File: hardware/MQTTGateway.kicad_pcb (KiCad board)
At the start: 2 copper layers, 284 parts, among them J1 Screw_Terminal_01x02, J10 Screw_Terminal_01x03, J11 Screw_Terminal_01x03, J12 Screw_Terminal_01x03, J13 Screw_Terminal_01x03, J14 Screw_Terminal_01x03, J15 Screw_Terminal_01x03, J16 Screw_Terminal_01x03, J17 Screw_Terminal_01x03, J18 Screw_Terminal_01x03, J19 Screw_Terminal_01x03, J2 RJ45_Amphenol_RJMG1BD3B8K1ANR, J20 Screw_Terminal_01x03, J21 Screw_Terminal_01x03, J22 Screw_Terminal_01x02, J23 Screw_Terminal_01x02, J24 Screw_Terminal_01x02, J25 Screw_Terminal_01x02, J3 Screw_Terminal_01x03, J4 Screw_Terminal_01x02, J5 Screw_Terminal_01x02, J6 Screw_Terminal_01x02, J7 Screw_Terminal_01x02, J8 Screw_Terminal_01x02, J9 Screw_Terminal_01x02, K1 G2RL-2, K2 G2RL-2, K3 G2RL-2, K4 G2RL-2, Q1 2N7002, Q2 2N7002, Q3 2N7002, Q4 2N7002, Q5 2N7002, Q6 2N7002, Q7 2N7002, Q8 2N7002, Q9 2N7002, SW1 SW_Push, U1 K78xx, U11 MCP6004, U15 LTV-847S, U2 AMS1117CD-3.3, U3 STM32F407VETx, U4 W25Q128JVS, U5 LAN8720A, U6 ESP32-WROOM-32E, U7 MAX3232, U8 SP3485CN, U9 SN65HVD230, Y1 8MHz, Y2 32.768 KHz, Y3 25MHz

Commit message: More improvements
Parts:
- removed U11 (x2): MCP6004, Package_DIP:SMDIP-16_W9.53mm
- added U10: MCP6004, Package_SO:SOIC-14_3.9x8.7mm_P1.27mm, F.Cu at (164.5, 148.4)
- moved D4 5.86 mm to (114.2, 105.2)

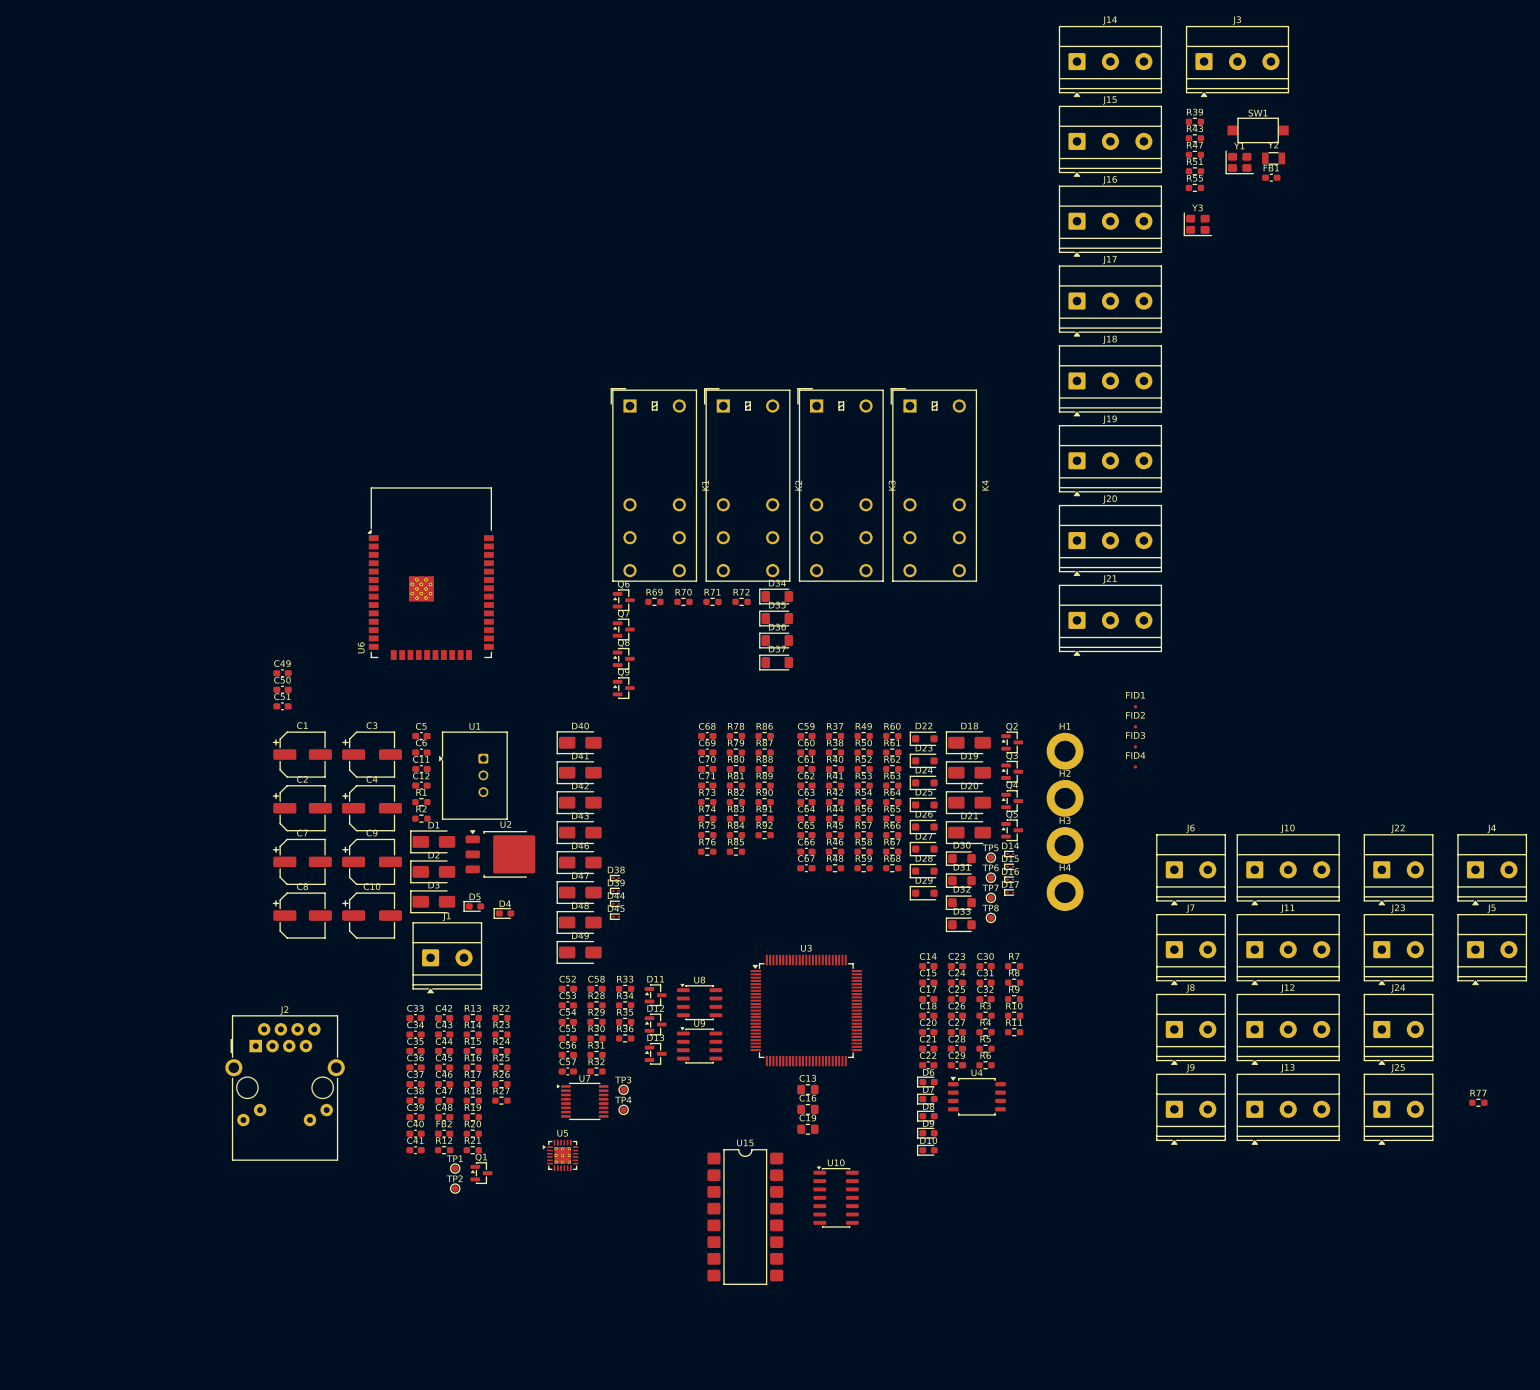
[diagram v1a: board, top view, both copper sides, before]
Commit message: Make connectors DB9
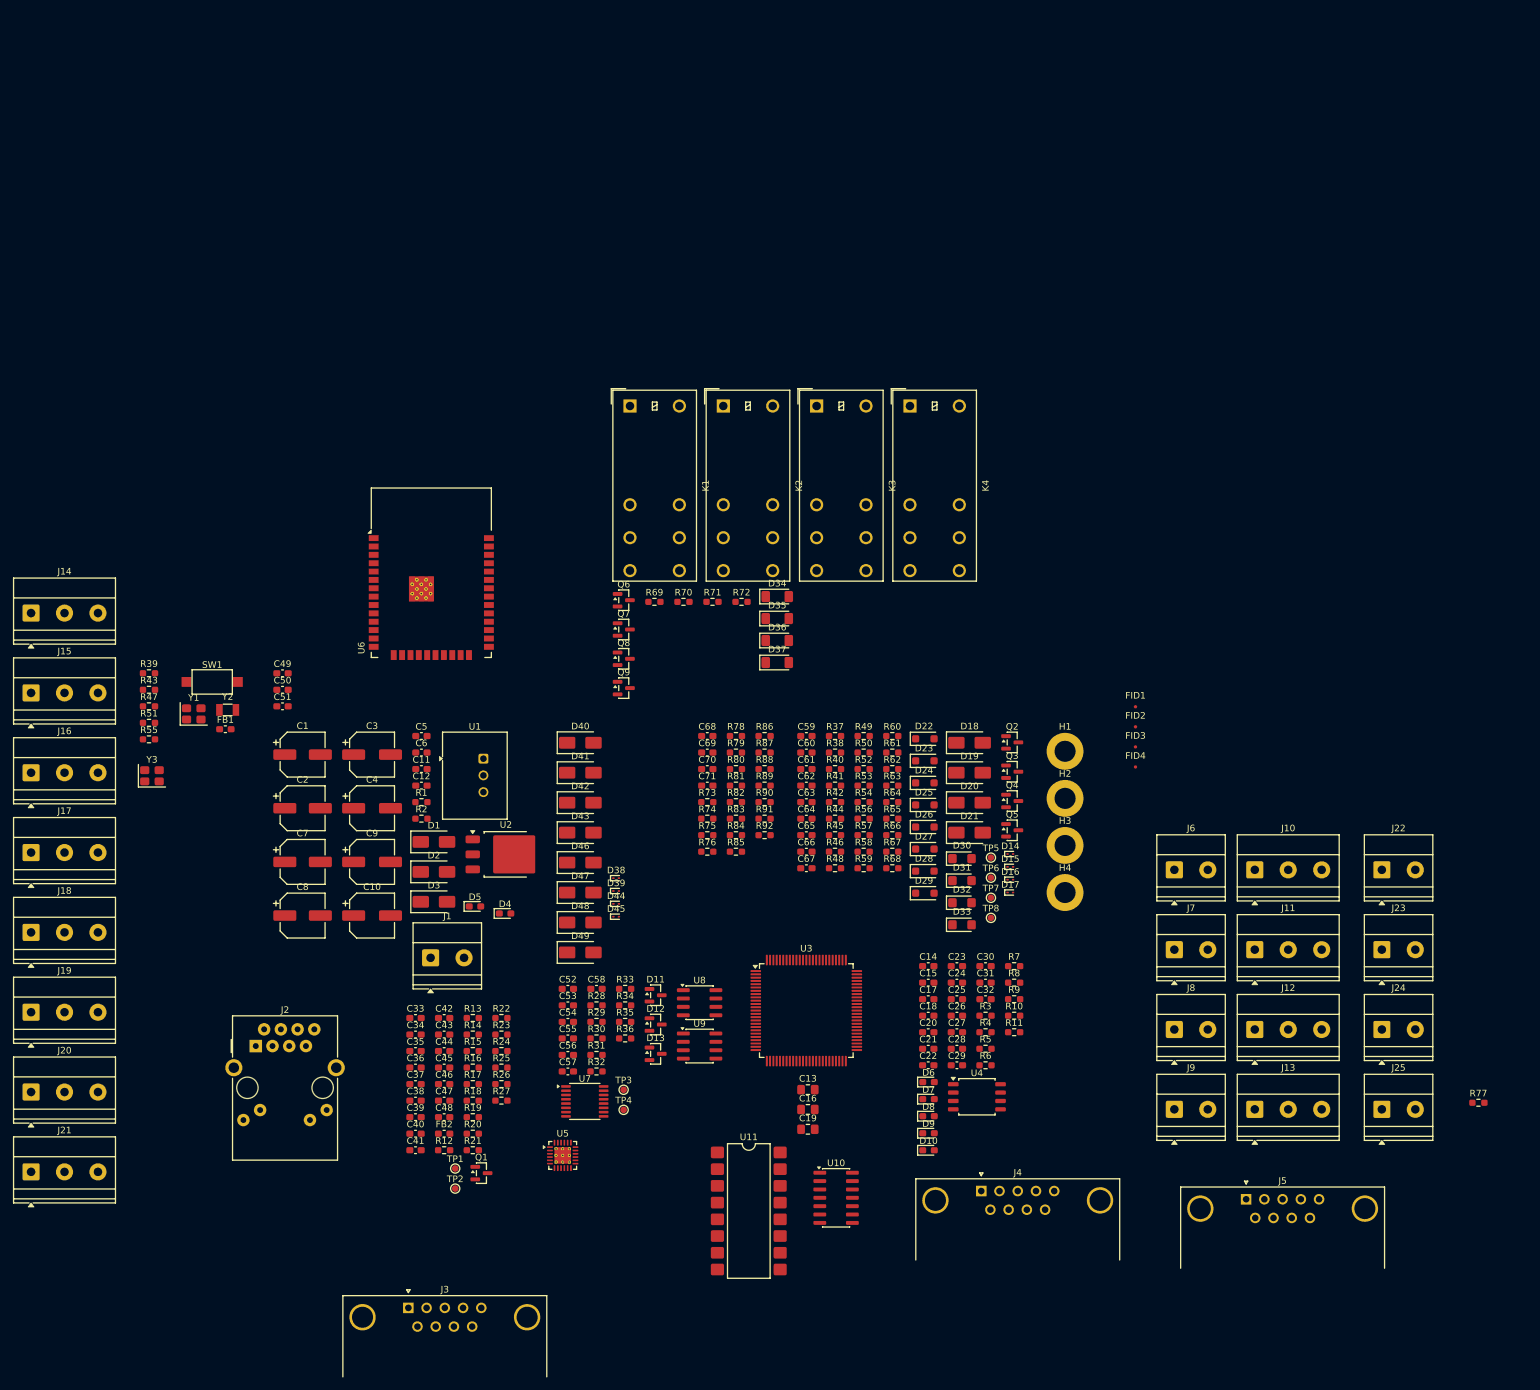
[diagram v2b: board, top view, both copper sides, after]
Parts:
- removed U15: LTV-847S, Package_DIP:SMDIP-16_W9.53mm
- added U11: LTV-847S, Package_DIP:SMDIP-16_W9.53mm, F.Cu at (151.3, 150.4)
- J3: value Screw_Terminal_01x03 -> DE9_Pins_MountingHoles; footprint TerminalBlock_Phoenix:TerminalBlock_Phoenix_MKDS-1,5-3-5.08_1x03_P5.08mm_Horizontal -> Connector_Dsub:DSUB-9_Pins_Horizontal_P2.77x2.84mm_EdgePinOffset7.70mm_Housed_MountingHolesOffset9.12mm
- J4, J5: value Screw_Terminal_01x02 -> DE9_Pins_MountingHoles; footprint TerminalBlock_Phoenix:TerminalBlock_Phoenix_MKDS-1,5-2-5.08_1x02_P5.08mm_Horizontal -> Connector_Dsub:DSUB-9_Pins_Horizontal_P2.77x2.84mm_EdgePinOffset7.70mm_Housed_MountingHolesOffset9.12mm
- moved J3 224.6 mm to (99.6, 165.2)
- moved FB1 179.6 mm to (71.8, 77.3)
- moved J14 179.6 mm to (42.2, 59.6)
- moved J15 179.6 mm to (42.2, 71.8)
- moved J16 179.6 mm to (42.2, 83.9)
- moved J17 179.6 mm to (42.2, 96.0)
- moved J18 179.6 mm to (42.2, 108.1)
- moved J19 179.6 mm to (42.2, 120.2)
- moved J20 179.6 mm to (42.2, 132.4)
- moved J21 179.6 mm to (42.2, 144.5)
- moved R39 179.6 mm to (60.2, 68.8)
- moved R43 179.6 mm to (60.2, 71.3)
- moved R47 179.6 mm to (60.2, 73.8)
- moved R51 179.6 mm to (60.2, 76.3)
- moved R55 179.6 mm to (60.2, 78.8)
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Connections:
- D11 pad 1: Net-(J3-Pin_1) -> /Peripherals/RS232_TX
- D11 pad 2: Net-(J3-Pin_3) -> /Peripherals/RS232_RX
- D12 pad 1: Net-(J4-Pin_1) -> /Peripherals/CAN_HIGH_P
- D12 pad 2: Net-(J4-Pin_2) -> /Peripherals/CAN_LOW_N
- D13 pad 1: Net-(D13-A1) -> /Peripherals/RS485_P
- D13 pad 2: Net-(D13-A2) -> /Peripherals/RS485_N
- J3 pad 1: Net-(J3-Pin_1) -> unconnected-(J3-Pad1)
- J3 pad 2: GND -> /Peripherals/RS232_RX
- J3 pad 3: Net-(J3-Pin_3) -> /Peripherals/RS232_TX
- J4 pad 1: Net-(J4-Pin_1) -> unconnected-(J4-Pad1)
- J4 pad 2: Net-(J4-Pin_2) -> unconnected-(J4-Pad2)
- J5 pad 1: Net-(D13-A1) -> unconnected-(J5-Pad1)
- J5 pad 2: Net-(D13-A2) -> /Peripherals/CAN_LOW_N
- R31 pad 2: Net-(J4-Pin_1) -> /Peripherals/CAN_HIGH_P
- R32 pad 1: Net-(J4-Pin_1) -> /Peripherals/CAN_HIGH_P
- R32 pad 2: Net-(J4-Pin_2) -> /Peripherals/CAN_LOW_N
- R33 pad 1: Net-(J4-Pin_2) -> /Peripherals/CAN_LOW_N
- R34 pad 2: Net-(D13-A1) -> /Peripherals/RS485_P
- R35 pad 1: Net-(D13-A1) -> /Peripherals/RS485_P
- R35 pad 2: Net-(D13-A2) -> /Peripherals/RS485_N
- R36 pad 1: Net-(D13-A2) -> /Peripherals/RS485_N
- U7 pad 13: Net-(J3-Pin_3) -> /Peripherals/RS232_RX
- U7 pad 14: Net-(J3-Pin_1) -> /Peripherals/RS232_TX
- U8 pad 6: Net-(D13-A1) -> /Peripherals/RS485_P
- U8 pad 7: Net-(D13-A2) -> /Peripherals/RS485_N
- U9 pad 6: Net-(J4-Pin_2) -> /Peripherals/CAN_LOW_N
- U9 pad 7: Net-(J4-Pin_1) -> /Peripherals/CAN_HIGH_P

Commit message: Improvements
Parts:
- added J26: Conn_01x07, Connector_Harwin:Harwin_M20-89007xx_1x07_P2.54mm_Horizontal, F.Cu at (-69.5, 318.5)
- moved R77 346.2 mm to (-72.7, 222.2)
- moved FID3 343.1 mm to (-45.8, 308.6)
- moved FID4 343.1 mm to (-45.8, 311.6)
- moved FID2 343.1 mm to (-45.8, 305.5)
- moved FID1 340.8 mm to (-47.6, 296.9)
- moved J19 275.2 mm to (-157.6, 309.4)
- moved C10 266.0 mm to (-128.0, 252.2)
- moved C11 266.0 mm to (-120.5, 229.9)
- moved C12 266.0 mm to (-120.5, 232.4)
- moved C13 266.0 mm to (-61.8, 278.6)
- moved C14 266.0 mm to (-43.5, 259.9)
- moved C15 266.0 mm to (-43.5, 262.4)
- moved C17 266.0 mm to (-43.5, 264.9)
- moved C2 266.0 mm to (-138.5, 235.9)
- moved C21 266.0 mm to (-43.5, 272.4)
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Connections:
- net Net-(U3-NRST) renamed /MCU/MCU_RESET
- U3 pad 35: /MCU/OUTPUT_ISO1 -> unconnected-(U3-PB0-Pad35)
- U3 pad 36: /MCU/OUTPUT_ISO2 -> unconnected-(U3-PB1-Pad36)
- U3 pad 37: /MCU/OUTPUT_ISO3 -> unconnected-(U3-PB2-Pad37)
- U3 pad 72: unconnected-(U3-PA13-Pad72) -> /MCU/SWDIO
- U3 pad 76: unconnected-(U3-PA14-Pad76) -> /MCU/SWCLK
- U3 pad 89: /MCU/OUTPUT_ISO4 -> /MCU/SWO
- U3 pad 92: unconnected-(U3-PB6-Pad92) -> /MCU/OUTPUT_ISO1
- U3 pad 93: unconnected-(U3-PB7-Pad93) -> /MCU/OUTPUT_ISO2
- U3 pad 95: unconnected-(U3-PB8-Pad95) -> /MCU/OUTPUT_ISO3
- U3 pad 96: unconnected-(U3-PB9-Pad96) -> /MCU/OUTPUT_ISO4
